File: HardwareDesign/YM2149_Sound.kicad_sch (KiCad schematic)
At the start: 20 parts, among them J801 Conn_01x02, J802 Conn_02x09_Odd_Even, J803 SJ1-3525N, U801 YM2149, U802 74HCT02, U803 74HCT04, U804 4 MHz

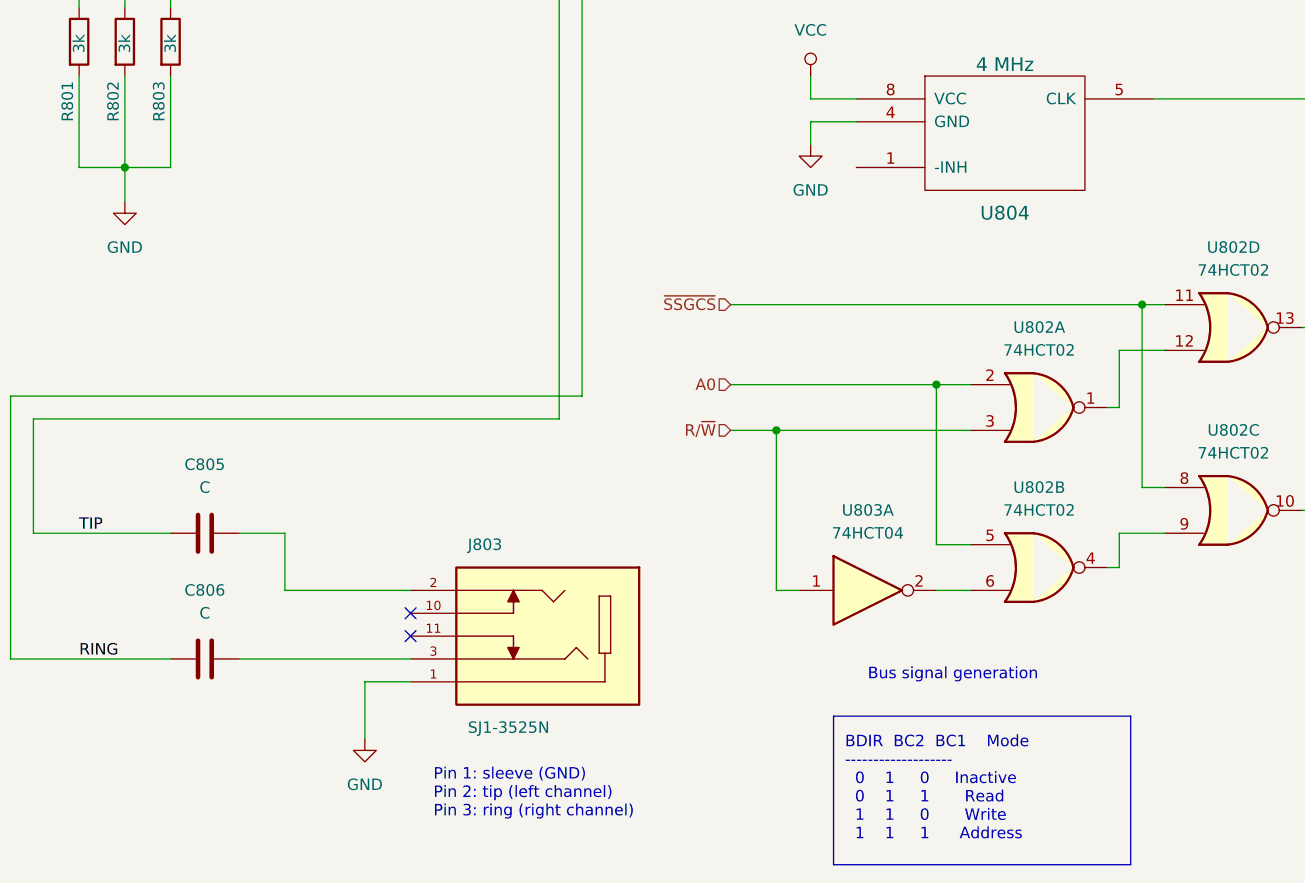
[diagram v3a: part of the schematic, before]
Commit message: values for audio coupling caps?
Need to prototype this
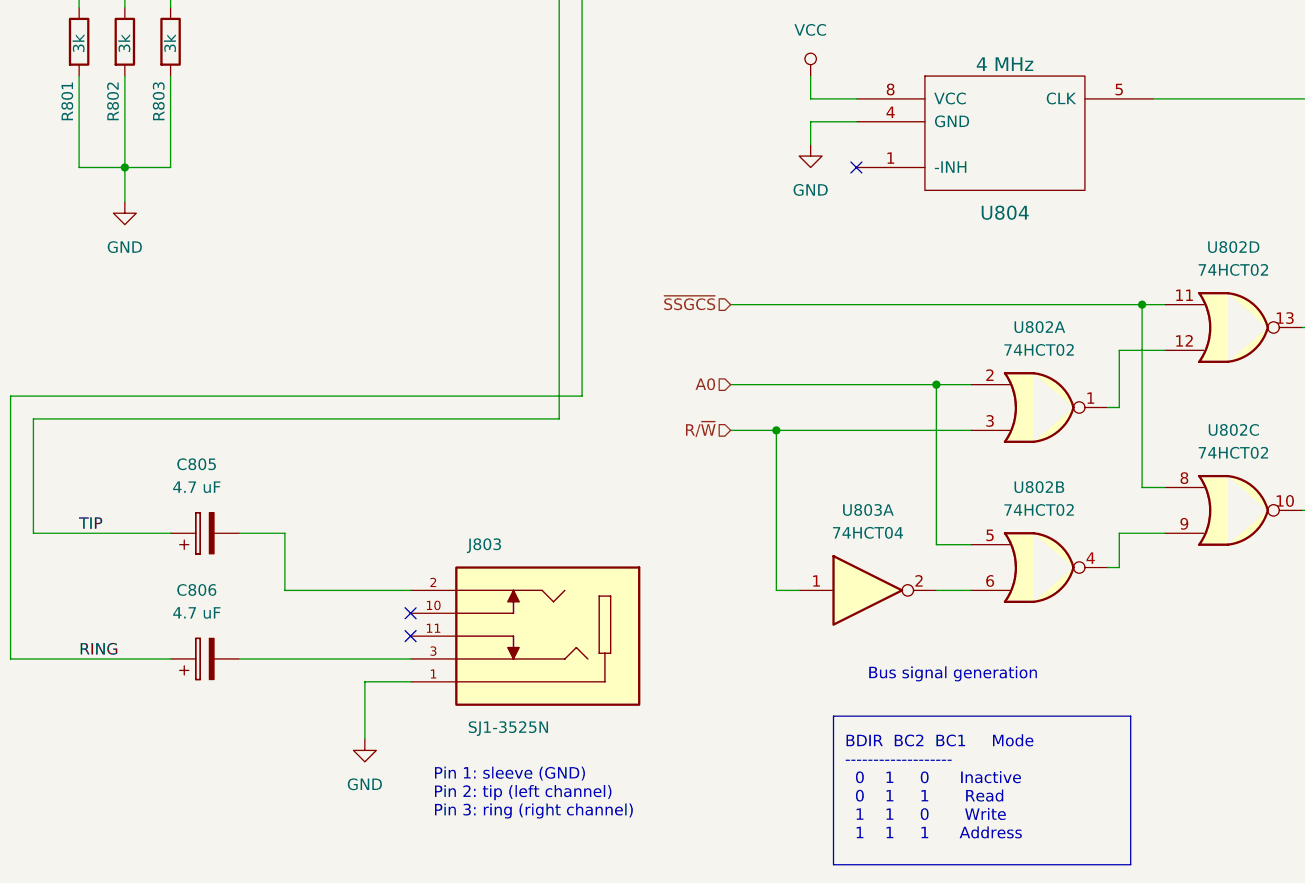
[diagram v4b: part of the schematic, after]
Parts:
- removed C805, C806: C, symbol device:C
- added C805, C806: 4.7 uF, symbol device:CP
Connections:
- net RING: now also C806.1
- net TIP: now also C805.1
- net at J803.2: now also C805.2
- net at J803.3: now also C806.2
- no-connect marks 11 -> 12
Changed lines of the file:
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@@
   (no_connect (at 153.67 78.74))
   (no_connect (at 67.31 163.83))
+  (no_connect (at 116.84 114.3))
   (no_connect (at 115.57 48.26))
   (no_connect (at 260.35 66.04))
@@
     (effects (font (size 1.27 1.27)) (justify left bottom))
   )
-  (text "BDIR  BC2  BC1    Mode\n-------------------\n  0    1     0     Inactive\n  0    1     1       Read\n  1    1     0       Write\n  1    1     1      Address"
+  (text "BDIR  BC2  BC1     Mode\n-------------------\n  0    1     0      Inactive\n  0    1     1       Read\n  1    1     0       Write\n  1    1     1      Address"
     (at 115.57 189.23 0)
     (effects (font (size 1.27 1.27)) (justify left bottom))
@@
     )
     (pin "1")
-  )
-  (symbol (lib_id "device:C") (at 44.45 154.94 90) (unit 1)
-    (in_bom yes) (on_board yes) (fields_autoplaced)
-    (property "Reference" "C805" (id 0) (at 44.45 147.32 90))
-    (property "Value" "C" (id 1) (at 44.45 149.86 90))
-    (property "Footprint" "" (id 2) (at 48.26 153.9748 0)
-      (effects (font (size 1.27 1.27)) hide)
-    )
-    (property "Datasheet" "" (id 3) (at 44.45 154.94 0)
-      (effects (font (size 1.27 1.27)) hide)
-    )
-    (pin "1")
-    (pin "2")
   )
   (symbol (lib_id "Device:R") (at 30.48 100.33 0) (unit 1)
@@
     (pin "2")
   )
-  (symbol (lib_id "device:C") (at 44.45 168.91 90) (unit 1)
-    (in_bom yes) (on_board yes) (fields_autoplaced)
-    (property "Reference" "C806" (id 0) (at 44.45 161.29 90))
-    (property "Value" "C" (id 1) (at 44.45 163.83 90))
-    (property "Footprint" "" (id 2) (at 48.26 167.9448 0)
-      (effects (font (size 1.27 1.27)) hide)
-    )
-    (property "Datasheet" "" (id 3) (at 44.45 168.91 0)
-      (effects (font (size 1.27 1.27)) hide)
-    )
-    (pin "1")
-    (pin "2")
-  )
   (symbol (lib_id "power:VCC") (at 231.14 139.7 0) (unit 1)
     (in_bom yes) (on_board yes) (fields_autoplaced)
@@
     )
     (pin "1")
+  )
+  (symbol (lib_id "device:CP") (at 44.45 154.94 90) (unit 1)
+    (in_bom yes) (on_board yes) (fields_autoplaced)
+    (property "Reference" "C805" (id 0) (at 43.561 147.32 90))
+    (property "Value" "4.7 uF" (id 1) (at 43.561 149.86 90))
+    (property "Footprint" "" (id 2) (at 48.26 153.9748 0)
+      (effects (font (size 1.27 1.27)) hide)
+    )
+    (property "Datasheet" "" (id 3) (at 44.45 154.94 0)
+      (effects (font (size 1.27 1.27)) hide)
+    )
+    (pin "1")
+    (pin "2")
   )
   (symbol (lib_id "power:VCC") (at 177.8 63.5 0) (unit 1)
@@
     (pin "7")
   )
+  (symbol (lib_id "device:CP") (at 44.45 168.91 90) (unit 1)
+    (in_bom yes) (on_board yes) (fields_autoplaced)
+    (property "Reference" "C806" (id 0) (at 43.561 161.29 90))
+    (property "Value" "4.7 uF" (id 1) (at 43.561 163.83 90))
+    (property "Footprint" "" (id 2) (at 48.26 167.9448 0)
+      (effects (font (size 1.27 1.27)) hide)
+    )
+    (property "Datasheet" "" (id 3) (at 44.45 168.91 0)
+      (effects (font (size 1.27 1.27)) hide)
+    )
+    (pin "1")
+    (pin "2")
+  )
   (symbol (lib_id "device:C") (at 238.76 148.59 0) (unit 1)

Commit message: connect backplane signals to YM2149 module
Also, tested the output circuit using 3.3 uF caps,
and it worked fine. 4.7 uF caps will probably also be
fine.
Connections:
- net ~{RST}: now reaches U801.23 (-RST)
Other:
- note added: "Note: this output circuit works well with 3.3 uF caps."
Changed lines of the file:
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@@
+    (stroke (width 0) (type default) (color 0 0 0 0))
+  )
+  (wire (pts (xy 153.67 81.28) (xy 165.1 81.28))
     (stroke (width 0) (type default) (color 0 0 0 0))
   )
@@
   )
   (text "Place jumper to halve\nclock frequency" (at 190.5 69.85 0)
+    (effects (font (size 1.27 1.27)) (justify left bottom))
+  )
+  (text "Note: this output circuit works\nwell with 3.3 uF caps."
+    (at 22.86 179.07 0)
     (effects (font (size 1.27 1.27)) (justify left bottom))
   )
@@
     (effects (font (size 1.27 1.27)) (justify right))
   )
+  (hierarchical_label "~{RST}" (shape input) (at 165.1 81.28 0)
+    (effects (font (size 1.27 1.27)) (justify left))
+  )
   (hierarchical_label "D1" (shape bidirectional) (at 165.1 48.26 0)

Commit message: 2.2 uF film caps seem to work well for audio coupling
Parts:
- removed C805, C806: 4.7 uF, symbol device:CP
- added C805, C806: 2.2 uF, symbol device:C
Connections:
- net RING: now also C806.1
- net TIP: now also C805.1
- net at J803.2: now also C805.2
- net at J803.3: now also C806.2
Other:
- note added: "2.2 uF film caps seem to work well here."
- note removed: "Note: this output circuit works well with 3.3 uF caps."
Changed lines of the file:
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@@
     (effects (font (size 1.27 1.27)) (justify left bottom))
   )
-  (text "Note: this output circuit works\nwell with 3.3 uF caps."
-    (at 22.86 179.07 0)
+  (text "2.2 uF film caps seem\nto work well here." (at 22.86 179.07 0)
     (effects (font (size 1.27 1.27)) (justify left bottom))
   )
@@
     (pin "1")
   )
-  (symbol (lib_id "device:CP") (at 44.45 154.94 90) (unit 1)
-    (in_bom yes) (on_board yes) (fields_autoplaced)
-    (property "Reference" "C805" (id 0) (at 43.561 147.32 90))
-    (property "Value" "4.7 uF" (id 1) (at 43.561 149.86 90))
-    (property "Footprint" "" (id 2) (at 48.26 153.9748 0)
-      (effects (font (size 1.27 1.27)) hide)
-    )
-    (property "Datasheet" "" (id 3) (at 44.45 154.94 0)
-      (effects (font (size 1.27 1.27)) hide)
-    )
-    (pin "1")
-    (pin "2")
-  )
   (symbol (lib_id "power:VCC") (at 177.8 63.5 0) (unit 1)
     (in_bom yes) (on_board yes) (fields_autoplaced)
@@
     )
     (property "Datasheet" "" (id 3) (at 58.42 86.36 0)
+      (effects (font (size 1.27 1.27)) hide)
+    )
+    (pin "1")
+    (pin "2")
+  )
+  (symbol (lib_id "device:C") (at 44.45 154.94 90) (unit 1)
+    (in_bom yes) (on_board yes) (fields_autoplaced)
+    (property "Reference" "C805" (id 0) (at 44.45 147.32 90))
+    (property "Value" "2.2 uF" (id 1) (at 44.45 149.86 90))
+    (property "Footprint" "" (id 2) (at 48.26 153.9748 0)
+      (effects (font (size 1.27 1.27)) hide)
+    )
+    (property "Datasheet" "" (id 3) (at 44.45 154.94 0)
       (effects (font (size 1.27 1.27)) hide)
     )
@@
     (pin "1")
   )
+  (symbol (lib_id "device:C") (at 44.45 168.91 90) (unit 1)
+    (in_bom yes) (on_board yes) (fields_autoplaced)
+    (property "Reference" "C806" (id 0) (at 44.45 161.29 90))
+    (property "Value" "2.2 uF" (id 1) (at 44.45 163.83 90))
+    (property "Footprint" "" (id 2) (at 48.26 167.9448 0)
+      (effects (font (size 1.27 1.27)) hide)
+    )
+    (property "Datasheet" "" (id 3) (at 44.45 168.91 0)
+      (effects (font (size 1.27 1.27)) hide)
+    )
+    (pin "1")
+    (pin "2")
+  )
   (symbol (lib_id "74xx:74HCT04") (at 252.73 100.33 0) (unit 5)
     (in_bom yes) (on_board yes) (fields_autoplaced)
@@
     (pin "7")
   )
-  (symbol (lib_id "device:CP") (at 44.45 168.91 90) (unit 1)
-    (in_bom yes) (on_board yes) (fields_autoplaced)
-    (property "Reference" "C806" (id 0) (at 43.561 161.29 90))
-    (property "Value" "4.7 uF" (id 1) (at 43.561 163.83 90))
-    (property "Footprint" "" (id 2) (at 48.26 167.9448 0)
-      (effects (font (size 1.27 1.27)) hide)
-    )
-    (property "Datasheet" "" (id 3) (at 44.45 168.91 0)
-      (effects (font (size 1.27 1.27)) hide)
-    )
-    (pin "1")
-    (pin "2")
-  )
   (symbol (lib_id "device:C") (at 238.76 148.59 0) (unit 1)
